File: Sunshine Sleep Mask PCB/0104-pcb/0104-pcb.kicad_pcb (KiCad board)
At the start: 2 copper layers, 8 parts, among them J1 Conn_01x02, J2 Conn_01x02, J3 Conn_01x04, J5 Conn_01x15, J6 Conn_01x15, U3 MAX98357A

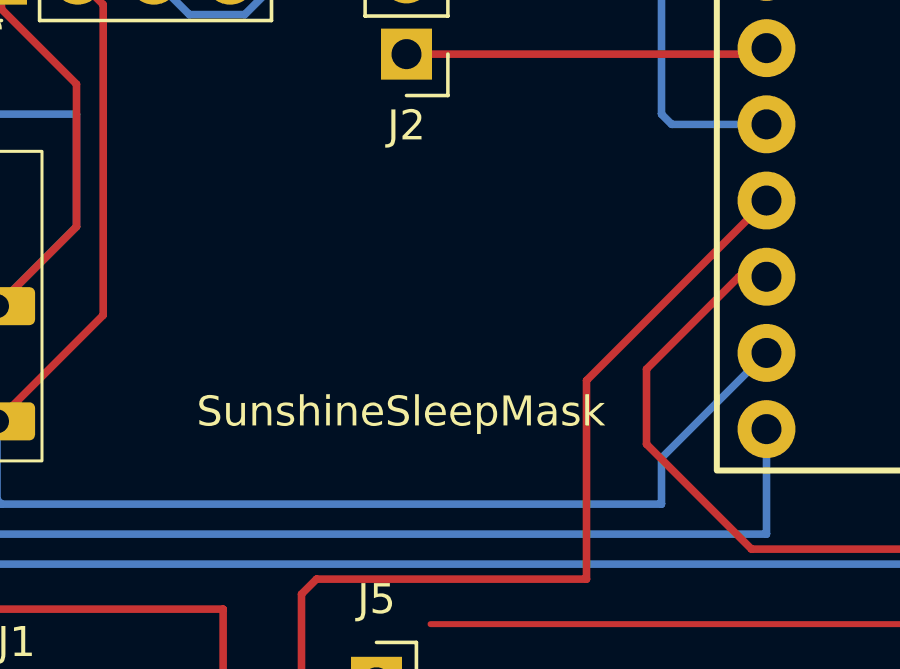
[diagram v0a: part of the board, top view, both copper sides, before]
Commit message: added the makers logo
makers logo in 0.3x0.3in
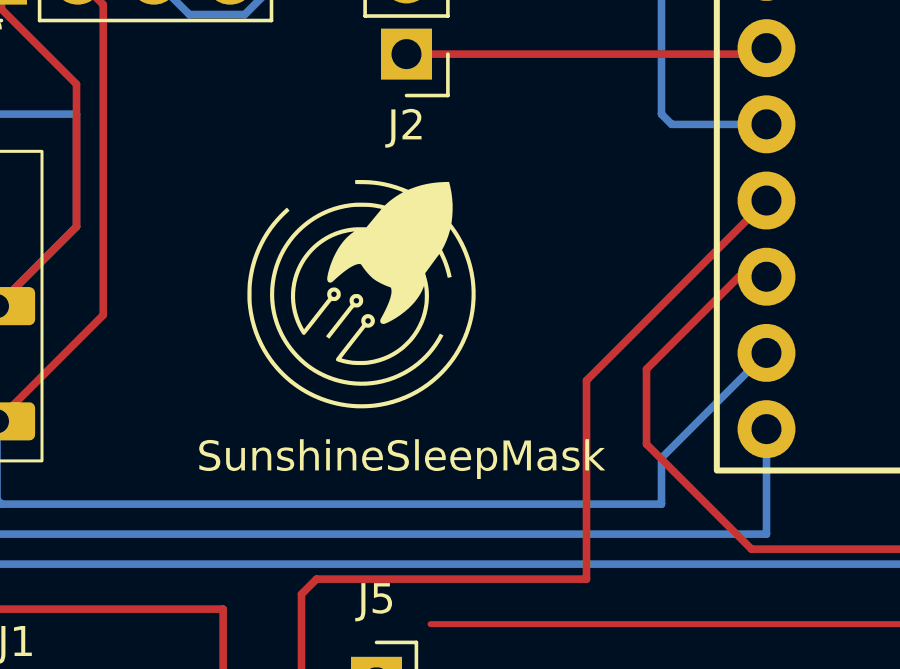
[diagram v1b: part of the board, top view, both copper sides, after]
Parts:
- added G***: LOGO, LOGO, F.Cu at (208.0, 68.0)

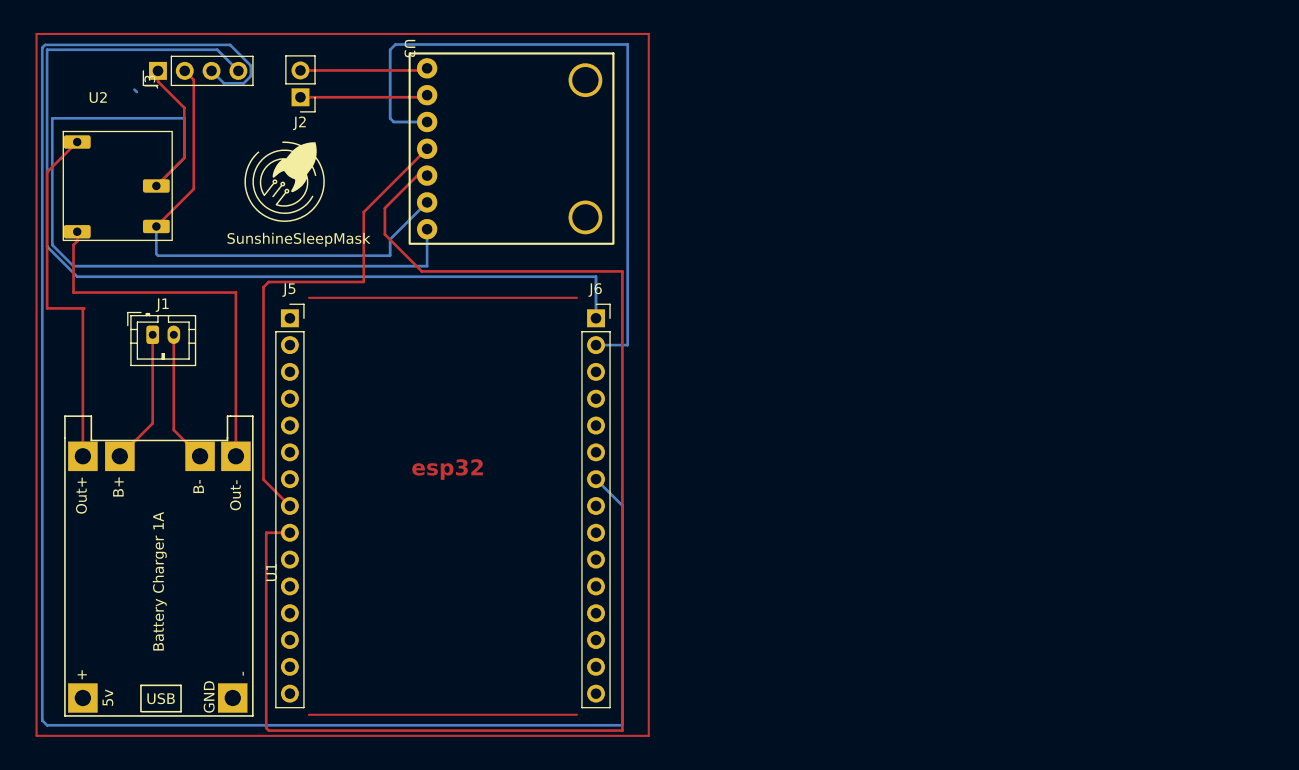
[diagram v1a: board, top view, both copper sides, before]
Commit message: GM
We meet with ray, we changed the wiring and we also realized we had issue with the pin connections
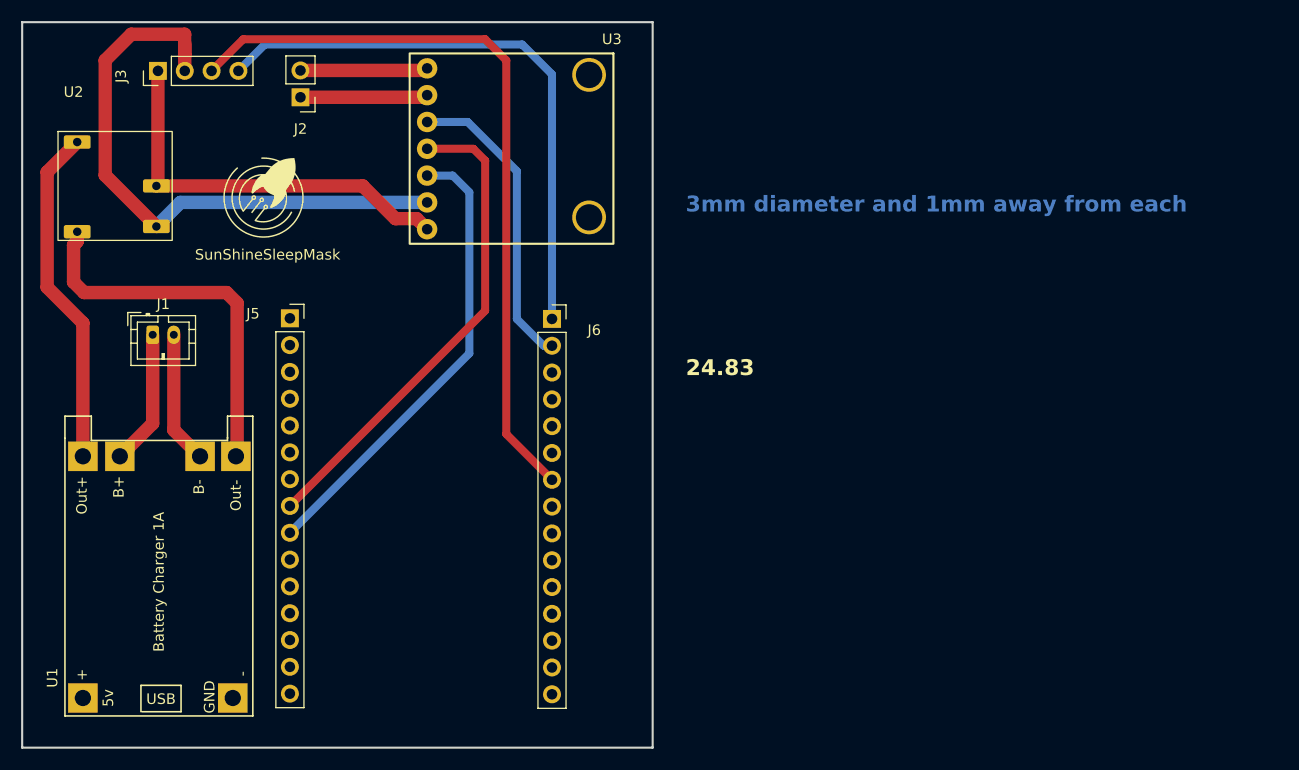
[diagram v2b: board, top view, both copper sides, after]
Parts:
- moved J6 4.17 mm to (233.3, 81.0)
- moved G*** 2.50 mm to (206.0, 69.5)
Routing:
- net Net-(J3-Pin_3): track 169.7 -> 71.5 mm
- net Net-(J5-Pin_9): track 129.8 -> 44.0 mm
- net Net-(J3-Pin_1): track 84.9 -> 38.3 mm
- net Net-(J3-Pin_4): track 94.7 -> 54.7 mm
- net Net-(J6-Pin_2): track 64.3 -> 28.8 mm
- net Net-(J3-Pin_2): track 47.9 -> 57.4 mm
- net Net-(U1-OUT_B+): track 34.5 -> 32.4 mm
- net Net-(U1-OUT_B-): track 36.8 -> 35.8 mm
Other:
- board outline added: 59.7 x 68.7 mm
- board text added: "24.83"
- board text added: "3mm diameter and 1mm away from each"
- board text added: "SunShineSleepMask"
- board text removed: "SunshineSleepMask"
- board text removed: "esp32"

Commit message: Clay 0408 Changes
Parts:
- removed J2: Conn_01x02, Connector_PinHeader_2.54mm:PinHeader_1x02_P2.54mm_Vertical
- removed J6: Conn_01x15, Connector_PinSocket_2.54mm:PinSocket_1x15_P2.54mm_Vertical
- J5: value Conn_01x15 -> ESP32_WROOM; footprint Connector_PinSocket_2.54mm:PinSocket_1x15_P2.54mm_Vertical -> RF_Module:ESP32_WROOM_DevKit_30Pin_Custom
- U2: footprint Library_customized_0104:boost_converter -> Library_customized_0104:Boost_Converter_Clay_Custom
- U3: footprint Library_customized_0104:amplifier_github -> Library_customized_0104:adafruit-MAX98357
- moved J5 150.8 mm to (59.7, 105.4), turned to 90 degrees
- moved G*** 141.6 mm to (64.4, 68.2)
- moved U3 117.1 mm to (119.0, 115.0)
- moved J3 114.0 mm to (82.5, 68.6)
- moved J1 83.9 mm to (112.3, 72.2), turned to -90 degrees
- moved U2 74.6 mm to (114.9, 93.1)
- moved U1 55.3 mm to (145.5, 82.2), turned to 180 degrees
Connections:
- J3 pad 2: Net-(J3-Pin_2) -> GND
- J5 pad 11: unconnected-(J5-Pin_11-Pad11) -> Net-(J3-Pin_3)
- J5 pad 13: unconnected-(J5-Pin_13-Pad13) -> Net-(J3-Pin_4)
- J5 pad 14: unconnected-(J5-Pin_14-Pad14) -> GND
- J5 pad 15: unconnected-(J5-Pin_15-Pad15) -> Net-(J3-Pin_1)
- J5 pad 8: Net-(J5-Pin_8) -> unconnected-(J5-GPIO25-Pad8)
- J5 pad 9: Net-(J5-Pin_9) -> unconnected-(J5-GPIO26-Pad9)
- U1 pad 1: (no net) -> unconnected-(U1-+R8-Pad1)
- U1 pad 2: (no net) -> unconnected-(U1-D-Pad2)
- U1 pad 4: Net-(U1-OUT_B-) -> GND
- U2 pad 2: Net-(U1-OUT_B-) -> GND
- U3 pad 2: Net-(J3-Pin_2) -> GND
- U3 pad 3: Net-(J5-Pin_9) -> unconnected-(U3-SV-Pad3)
- U3 pad 4: Net-(J5-Pin_8) -> unconnected-(U3-GAIN-Pad4)
- U3 pad 5: Net-(J6-Pin_2) -> Net-(J5-GPIO4)
- U3 pad 6: Net-(J2-Pin_1) -> Net-(J5-GPIO2)
- U3 pad 7: Net-(J2-Pin_2) -> Net-(J5-GPIO15)
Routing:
- net Net-(J3-Pin_1): track 38.3 -> 143.2 mm
- net Net-(J3-Pin_2): track 57.4 -> 0.00 mm
- net Net-(J3-Pin_3): track 71.5 -> 15.0 mm
- net Net-(J5-Pin_8): track 46.3 -> 0.00 mm
- net Net-(J5-Pin_9): track 44.0 -> 0.00 mm
- net Net-(J3-Pin_4): track 54.7 -> 14.0 mm
- net Net-(J5-GPIO4): track 0.00 -> 36.9 mm
- net Net-(U1-OUT_B-): track 35.8 -> 0.00 mm
- net Net-(J5-GPIO2): track 0.00 -> 30.5 mm
- net Net-(J6-Pin_2): track 28.8 -> 0.00 mm
- net -V: track 12.5 -> 41.0 mm
- net Net-(J5-GPIO15): track 0.00 -> 25.7 mm
- net Net-(U1-OUT+): track 32.4 -> 16.3 mm
- net Net-(J2-Pin_2): track 12.1 -> 0.00 mm
- net Net-(J2-Pin_1): track 12.1 -> 0.00 mm
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- added copper zone on B.Cu, net GND
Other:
- board size 59.7 x 68.7 mm -> 99.2 x 74.7 mm
- board text added: "SunshineSleepMask"
- board text removed: "24.83"
- board text removed: "3mm diameter and 1mm away from each"
- board text removed: "SunShineSleepMask"
